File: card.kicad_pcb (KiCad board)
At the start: 2 copper layers, 89 x 51 mm, 22 parts, among them J1 Conn_01x08, J2 Conn_01x04, J3 Conn_01x04, SW1 SW_SPDT, U1 ISP1907, U2 MTCH6102

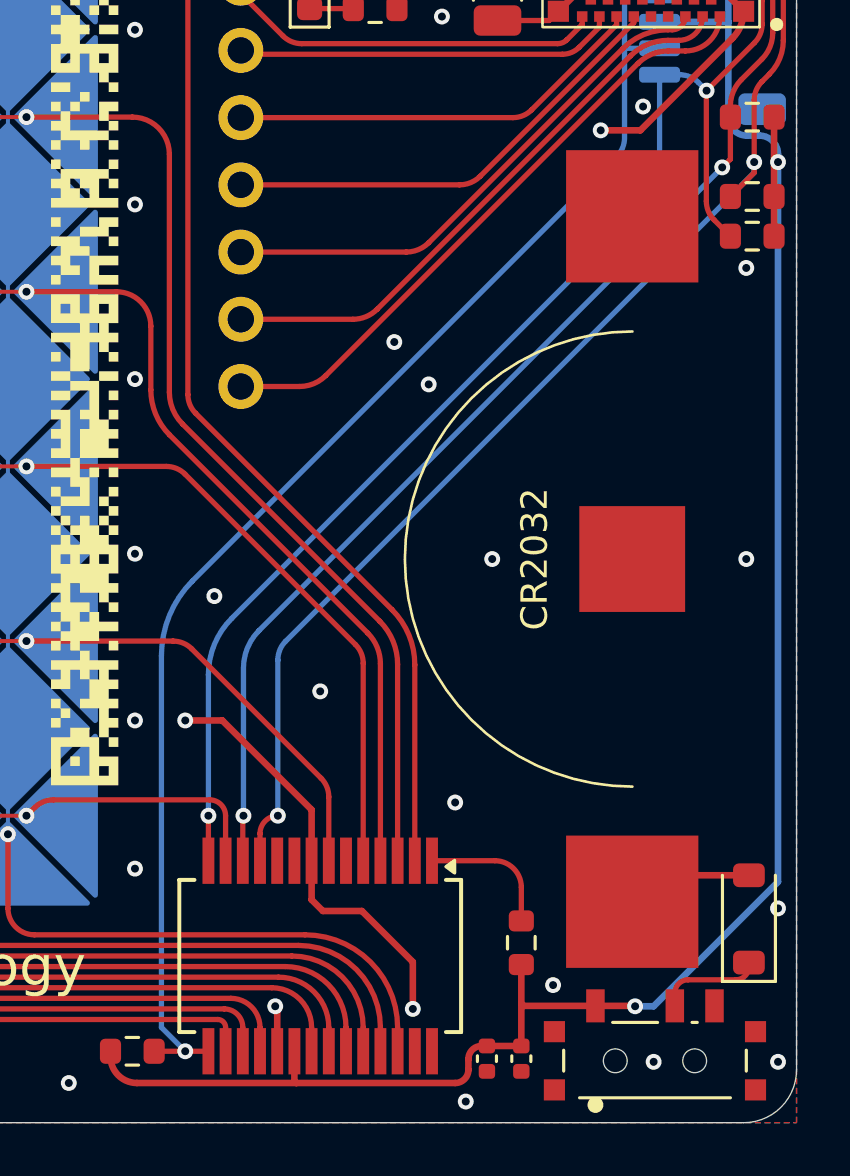
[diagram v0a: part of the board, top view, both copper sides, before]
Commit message: add teardrops
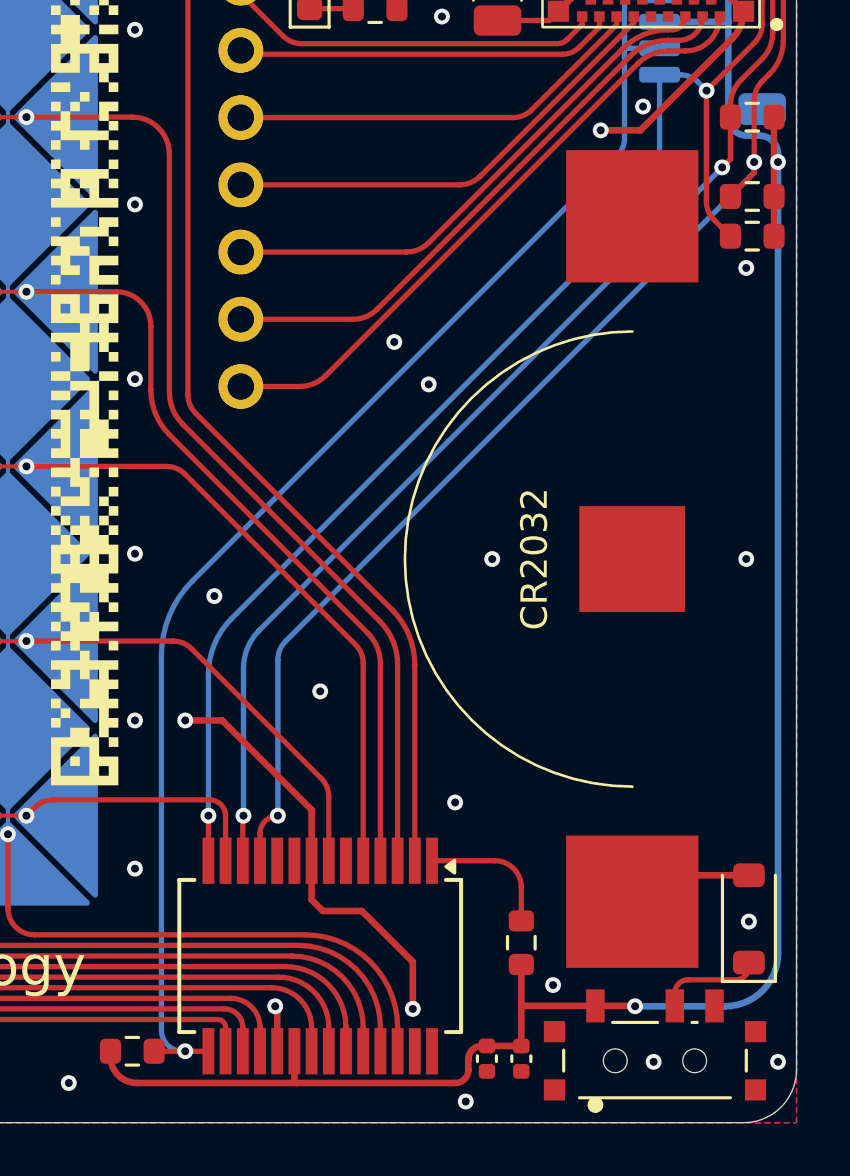
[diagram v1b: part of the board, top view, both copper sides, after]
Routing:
- net +BATT: track 103.3 -> 105.1 mm
